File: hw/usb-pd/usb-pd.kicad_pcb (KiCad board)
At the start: 4 copper layers, 42 parts, among them J1 +BAT, J2 PGM_I2C, J3 USB_C_Receptacle_USB2.0, Q1 BSS138, Q2 TPCC8105L1Q, Q3 TPCC8105L1Q, U1 STUSB4710AQ1, U2 MAX25240

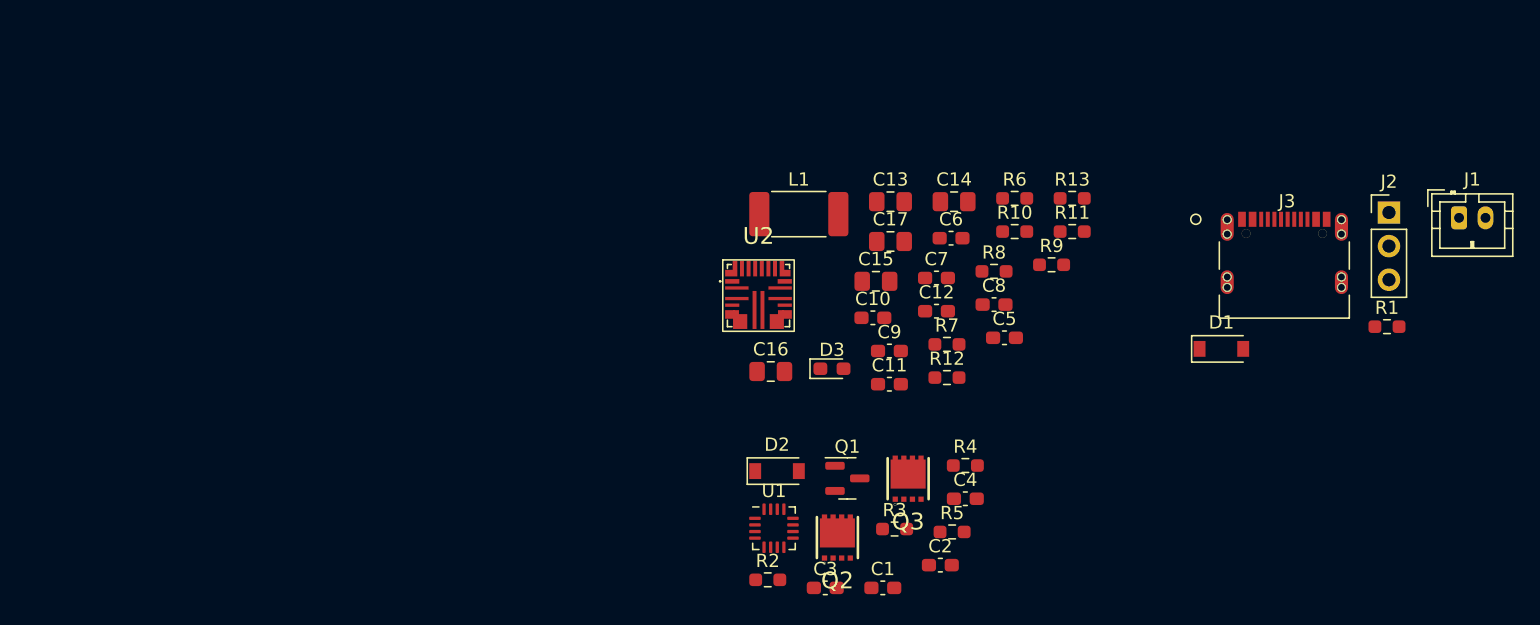
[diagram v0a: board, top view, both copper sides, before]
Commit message: Preliminary PCB layout, calculated compensation filter and feedback network for MAX25240
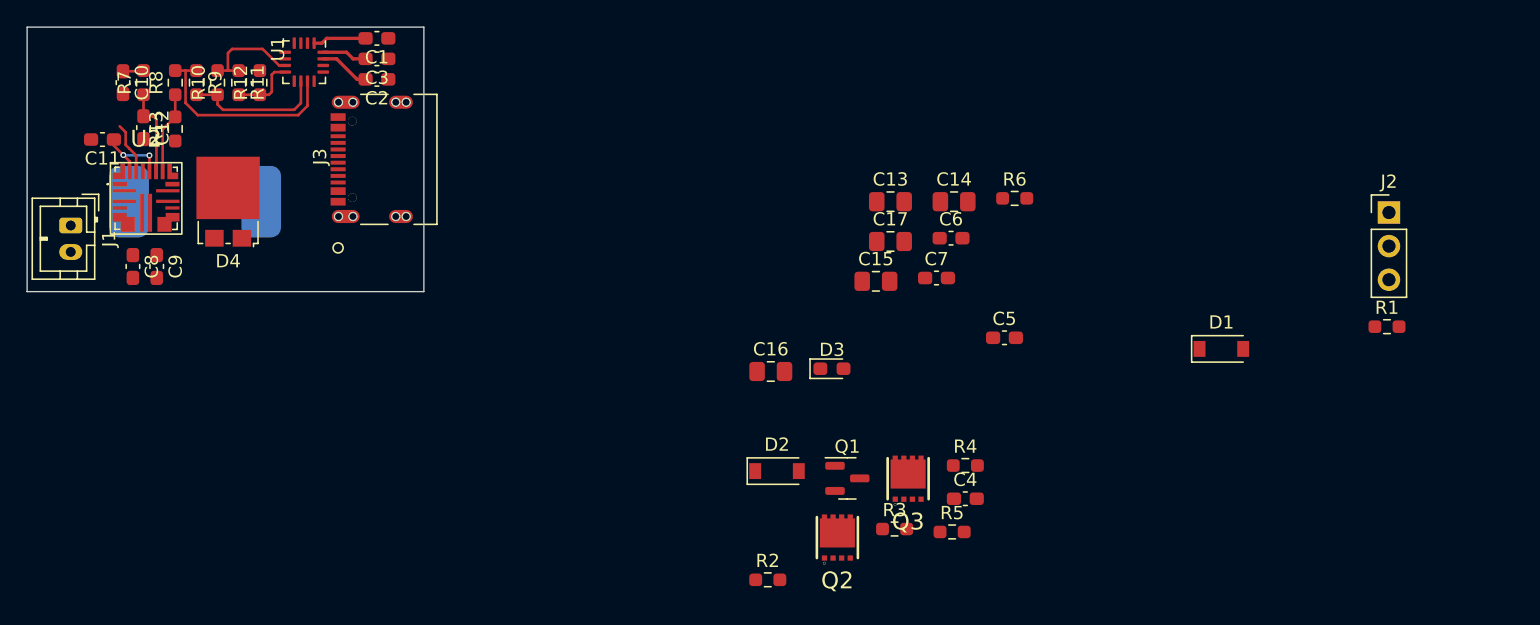
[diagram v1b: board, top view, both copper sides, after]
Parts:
- added D4: V8PL6-M3/86A, footprints:TMBS-TO-277A, F.Cu at (85.2, 53.2)
- L1: value L_Small -> 10uH 8.4A; footprint Inductor_SMD:L_2512_6332Metric_Pad1.52x3.35mm_HandSolder -> footprints:BPSC00131380100M00; moved to B.Cu
- moved J1 105.0 mm to (73.3, 55.0), turned to -90 degrees
- moved J3 68.5 mm to (97.0, 50.0), turned to 90 degrees
- moved R13 68.0 mm to (81.2, 47.7), turned to 90 degrees
- moved R9 66.1 mm to (82.8, 44.2), turned to -90 degrees
- moved C8 65.2 mm to (78.0, 58.1), turned to -90 degrees
- moved R11 64.0 mm to (86.0, 44.2), turned to -90 degrees
- moved R7 63.9 mm to (78.8, 44.2), turned to 90 degrees
- moved R8 63.5 mm to (81.2, 44.2), turned to 90 degrees
- moved C11 62.3 mm to (75.7, 48.5), turned to 180 degrees
- moved C12 61.5 mm to (78.8, 47.6), turned to -90 degrees
- moved R10 61.3 mm to (84.4, 44.2), turned to 90 degrees
- moved C10 59.4 mm to (77.2, 44.2), turned to -90 degrees
- moved R12 56.5 mm to (87.6, 44.2), turned to 90 degrees
- moved C1 56.5 mm to (96.5, 40.9), turned to 180 degrees
- moved C2 56.2 mm to (96.5, 44.0), turned to 180 degrees
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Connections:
- U2 pad 18: (no net) -> Net-(C11-Pad1)
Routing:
- net /USB-PD Negotiator/PDO5: track 0.00 -> 15.8 mm
- net /USB-PD Negotiator/PDO4: track 0.00 -> 10.7 mm
- net /USB-PD Negotiator/PDO3: track 0.00 -> 7.90 mm
- net Net-(C12-Pad1): track 0.00 -> 6.65 mm
- net Net-(R13-Pad2): track 0.00 -> 6.19 mm
- net Net-(C11-Pad1): track 0.00 -> 6.10 mm, vias 0 -> 2
- net /USB-PD Negotiator/PDO2: track 0.00 -> 4.98 mm
- net /USB-PD Negotiator/Vin: track 0.00 -> 4.04 mm
- net Net-(D3-Pad1): track 0.00 -> 3.93 mm
- net Net-(C2-Pad2): track 0.00 -> 3.84 mm
- net Net-(C3-Pad2): track 0.00 -> 3.41 mm
- net Net-(C10-Pad1): track 0.00 -> 1.57 mm
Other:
- board outline added: 30 x 20 mm
